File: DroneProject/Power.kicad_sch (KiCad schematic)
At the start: 15 parts, among them SW1 PTS815 SJM 250 SMTR LFS, U31 AP63205WU, U32 TLV75533PDBV

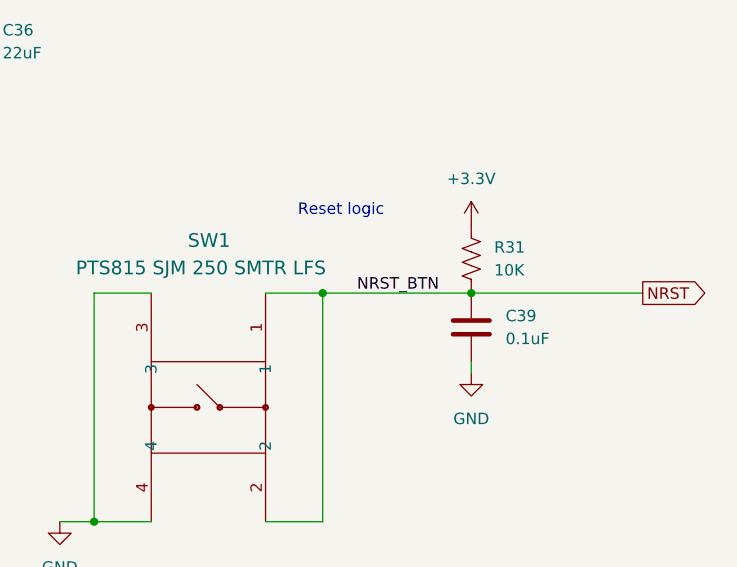
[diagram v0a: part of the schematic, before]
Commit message: Added mounting holes and some more testpoints.  Also started on PCB with dimesions and mounting holes measured and placed
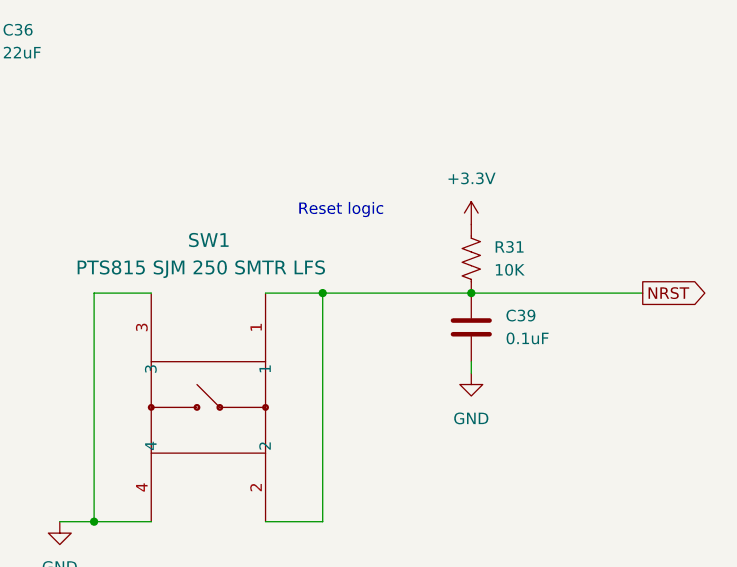
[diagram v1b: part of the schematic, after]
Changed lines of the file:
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@@
-		)
-	)
-	(label "NRST_BTN"
-		(at 212.09 76.2 0)
-		(effects
-			(font
-				(size 1.27 1.27)
-			)
-			(justify left bottom)
 		)
 	)

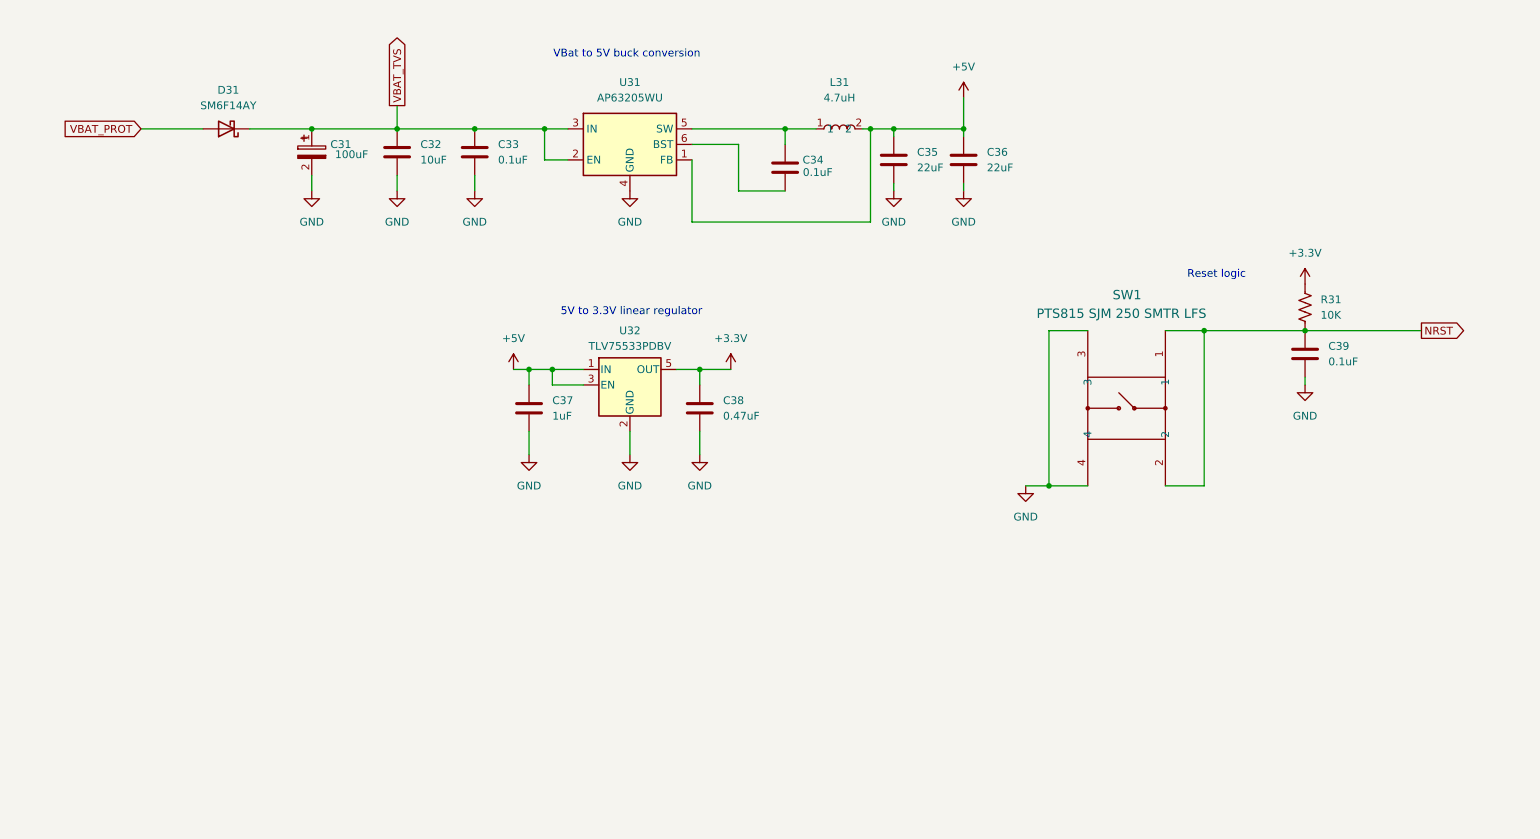
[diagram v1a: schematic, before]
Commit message: Finished initial PCB layout.  However decided to go ahead and add the motor drivers for the first prototype anyways.  Re-did the reverse-polarity detection to use an NMOS instead of a PMOS.  Added sheets for each motor, still need to decide on parts.
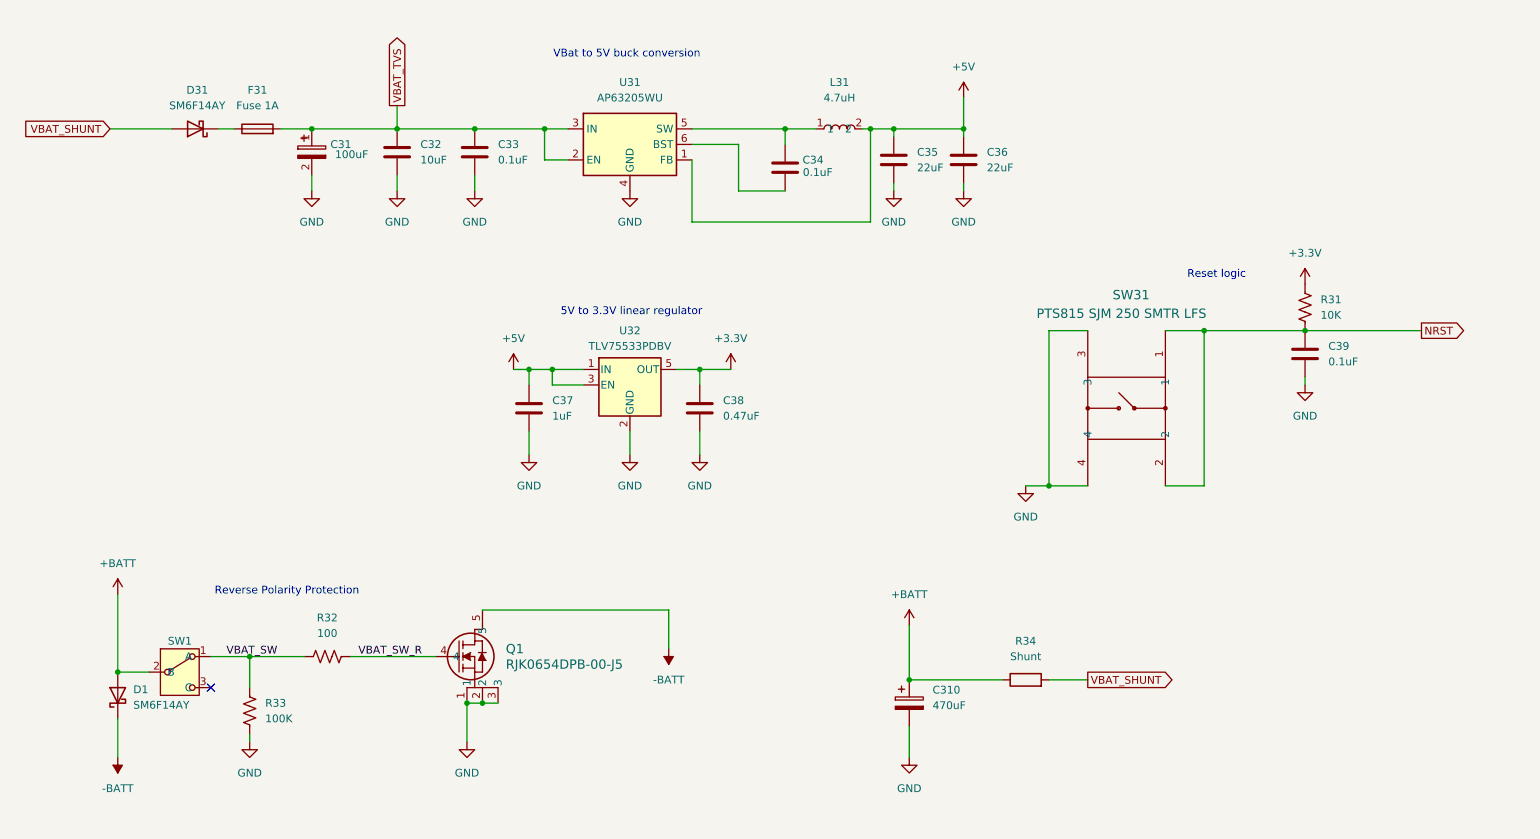
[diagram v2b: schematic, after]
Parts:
- added C310: 470uF, Capacitor_SMD:CP_Elec_10x10.5, symbol Device:C_Polarized
- added D1: SM6F14AY, Diode_SMD:D_SOD-128, symbol Diode:PMEG4050EP
- added F31: Fuse 1A, Fuse:Fuse_1812_4532Metric, symbol Device:Fuse
- added Q1: RJK0654DPB-00-J5, Library:LFPAK_REN, symbol Global:RJK0654DPB-00-J5
- added R32: 100, Resistor_SMD:R_0201_0603Metric, symbol Device:R_US
- added R33: 100K, Resistor_SMD:R_0402_1005Metric, symbol Device:R_US
- added R34: Shunt, Resistor_SMD:R_2010_5025Metric, symbol Device:R
- added SW1: ~, Library:SW_EG1218, symbol Global:EG1903-ND
- renumbered SW1 to SW31
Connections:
- net GND: now also C310.2, Q1.1, Q1.2, Q1.3, R33.2
- net VBAT_TVS: now also F31.2; no longer D31.1 (K)
- net VBAT_PROT renamed VBAT_SHUNT
- net VBAT_SHUNT: now also R34.2
- new net: D31.1 (K), F31.1
- new net +BATT: C310.1, D1.2 (A), R34.1, SW1.2 (B)
- new net -BATT: D1.1 (K), Q1.5
- new net VBAT_SW: R32.1, R33.1, SW1.1 (A)
- new net VBAT_SW_R: Q1.4, R32.2
- no-connect marks 0 -> 1
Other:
- note added: "Reverse Polarity Protection"
- moved on the sheet: D31

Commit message: Re-did layout for new power system
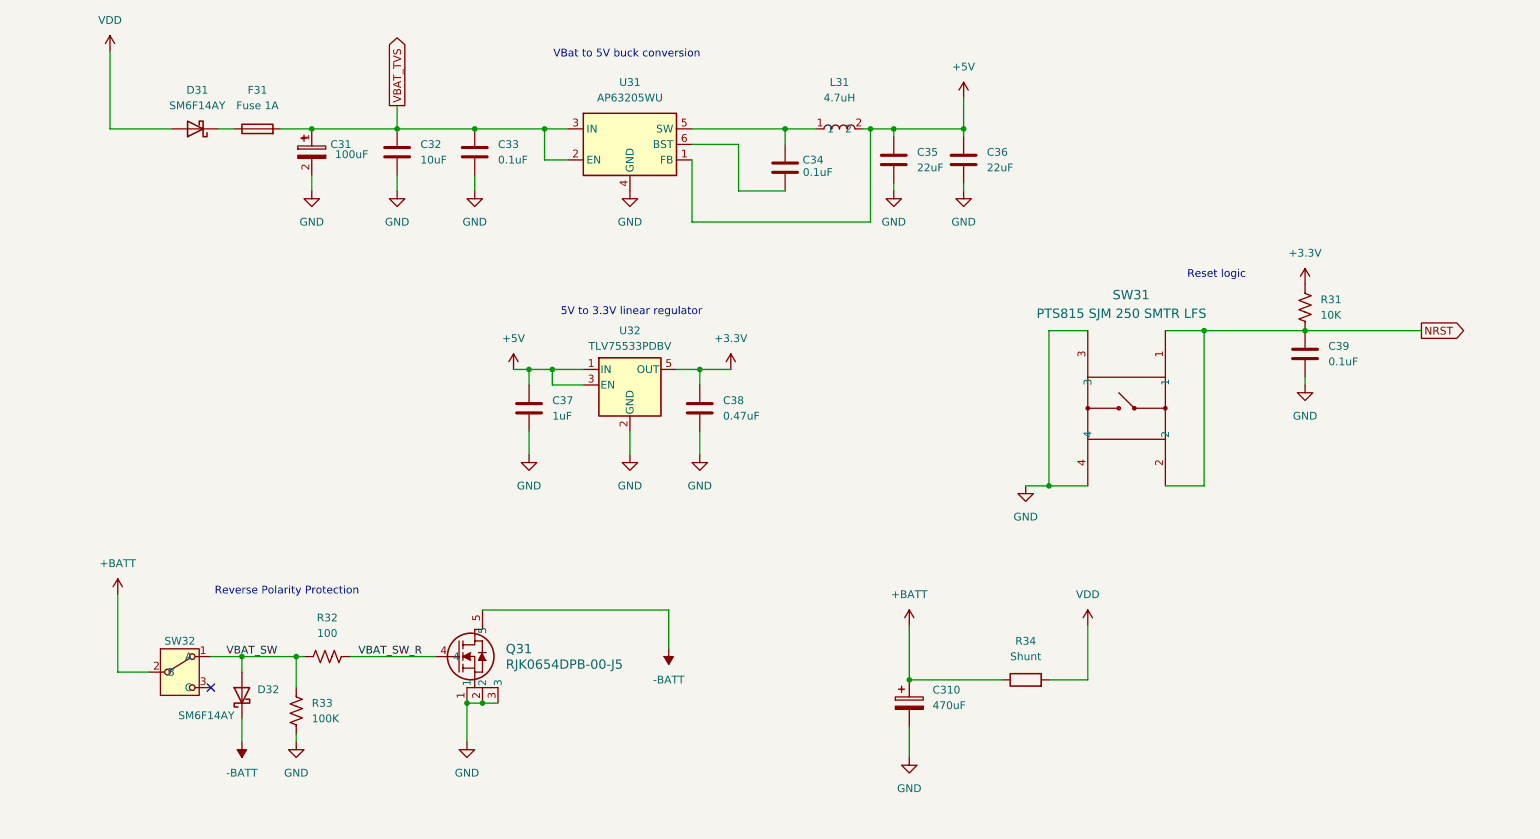
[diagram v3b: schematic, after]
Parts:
- renumbered D1 to D32, Q1 to Q31, SW1 to SW32
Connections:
- net +BATT: no longer D32.2 (A)
- net VBAT_SW: now also D32.2 (A)
- net VBAT_SHUNT renamed VDD
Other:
- moved on the sheet: D32, R33

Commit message: Added a second MCU for motor control.  Removed 5V rail.  Added COM switching for SWD and UART external headers
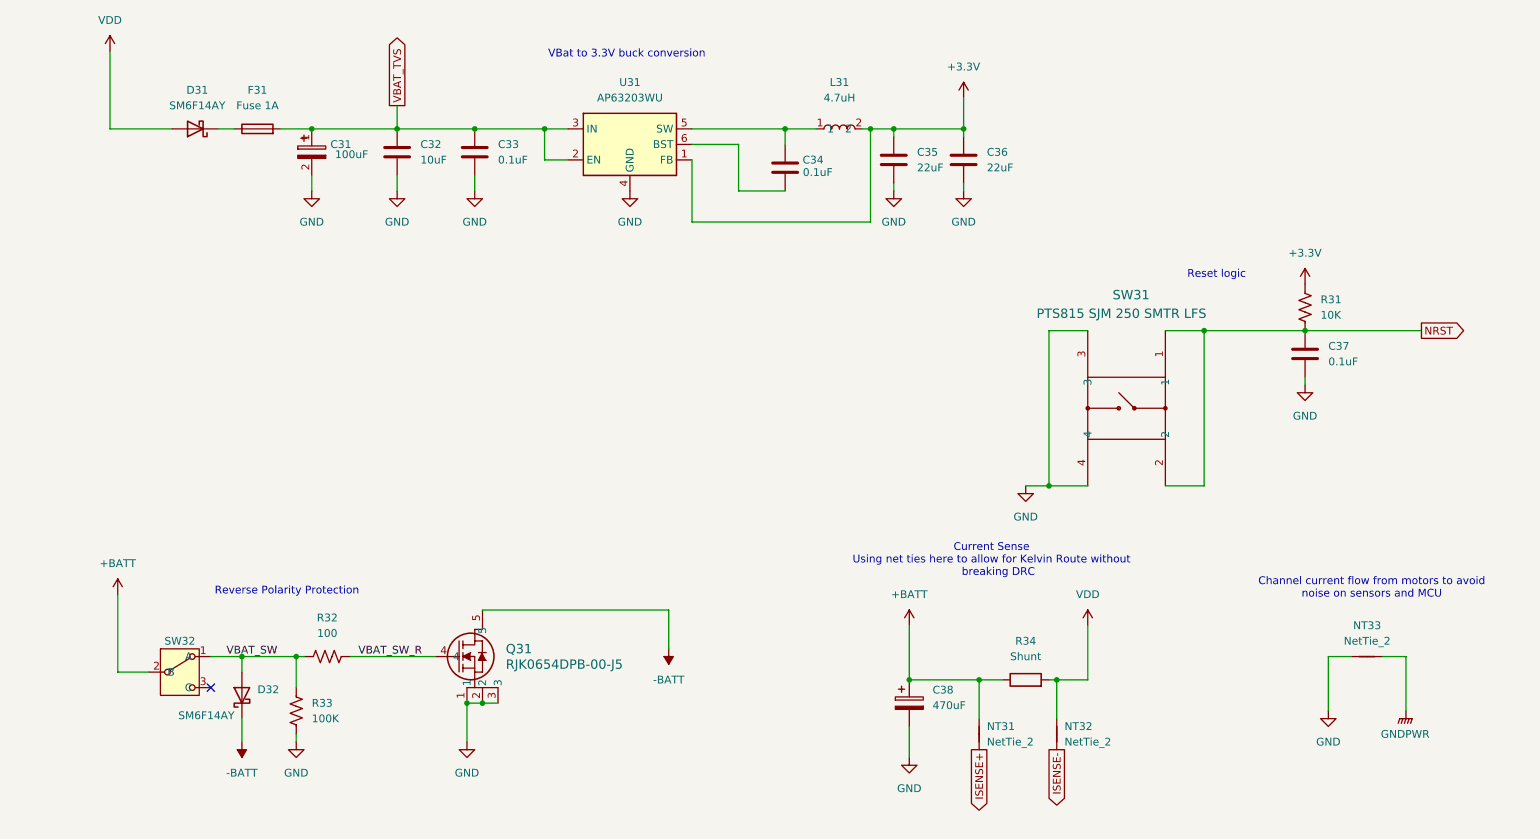
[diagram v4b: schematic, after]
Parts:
- removed C37: 1uF, Capacitor_SMD:C_0402_1005Metric, symbol Device:C
- removed C38: 0.47uF, Capacitor_SMD:C_0402_1005Metric, symbol Device:C
- removed U31: AP63205WU, Package_TO_SOT_SMD:TSOT-23-6, symbol Regulator_Switching:AP63205WU
- removed U32: TLV75533PDBV, Package_TO_SOT_SMD:SOT-23-5, symbol Regulator_Linear:TLV75533PDBV
- added NT31, NT32: NetTie_2, NetTie:NetTie-2_SMD_Pad0.5mm, symbol Device:NetTie_2
- added NT33: NetTie_2, NetTie:NetTie-2_SMD_Pad2.0mm, symbol Device:NetTie_2
- added U31: AP63203WU, Package_TO_SOT_SMD:TSOT-23-6, symbol Regulator_Switching:AP63203WU
- renumbered C39 to C37, C310 to C38
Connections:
- net +5V is gone; now on net +3.3V: C35.1, C36.1, L31.2
- net +3.3V: now also U31.1 (FB)
- net +BATT: now also NT31.2
- net GND: now also NT33.2, U31.4 (GND)
- net VBAT_TVS: now also U31.2 (EN), U31.3 (IN)
- net VDD: now also NT32.2
- net at C34.2, L31.1: now also U31.5 (SW)
- net at C34.1: now also U31.6 (BST)
- new net GNDPWR: NT33.1
- new net ISENSE+: NT31.1
- new net ISENSE-: NT32.1
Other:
- note added: "Channel current flow from motors to avoid noise on sensors and MCU"
- note added: "Current Sense Using net ties here to allow for Kelvin Route without breaking DRC"
- note added: "VBat to 3.3V buck conversion"
- note removed: "5V to 3.3V linear regulator"
- note removed: "VBat to 5V buck conversion"

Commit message: Removed C1 and motor controllers from main platform and moved to own project
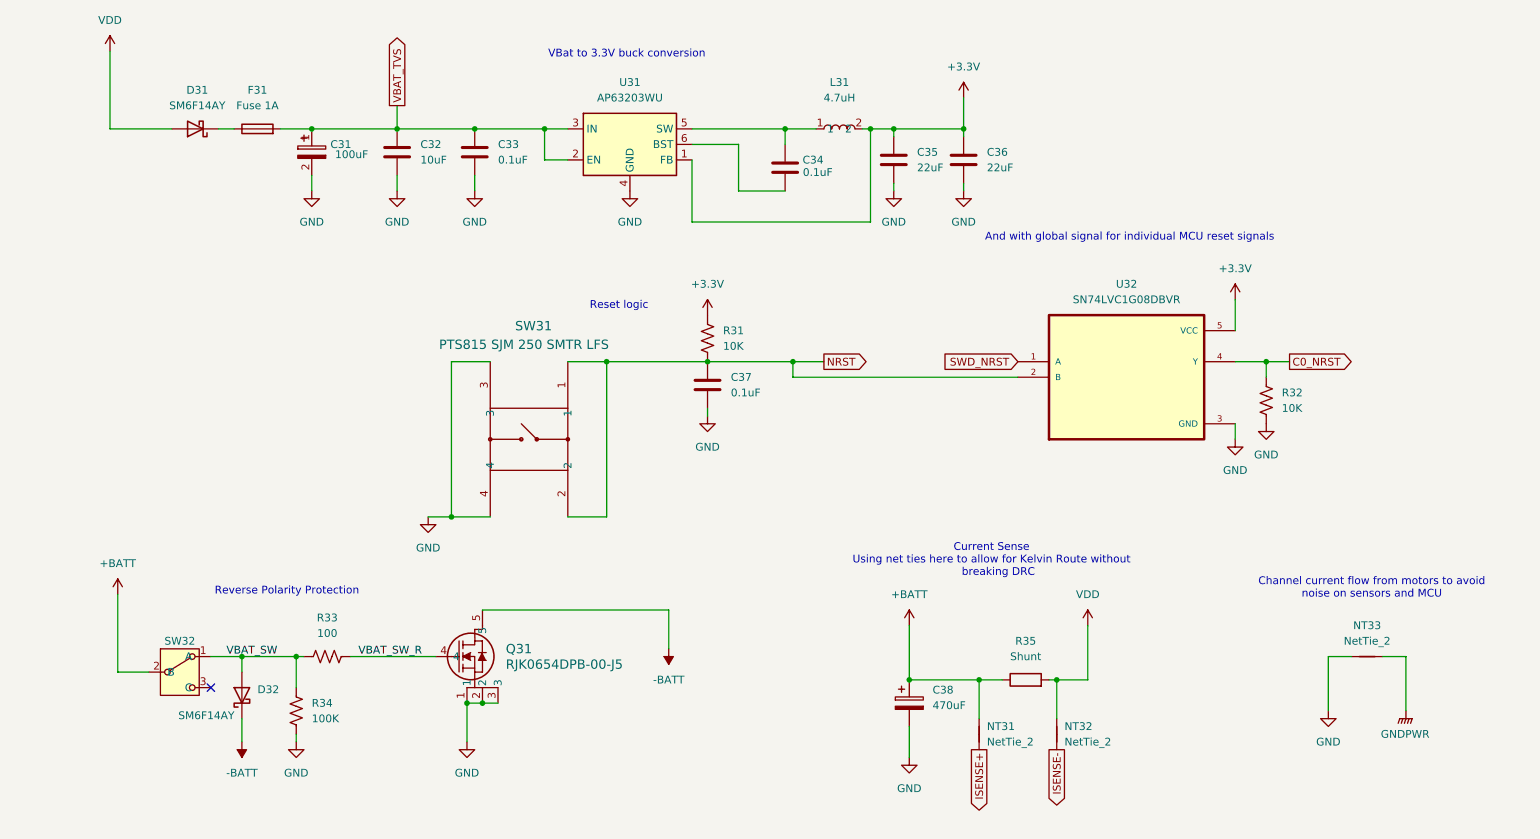
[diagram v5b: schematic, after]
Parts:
- added R32: 10K, Resistor_SMD:R_0402_1005Metric, symbol Device:R_US
- added U32: SN74LVC1G08DBVR, Library:SOT95P280X145-5N, symbol Global:SN74LVC1G08DBVR
- renumbered R32 to R33, R33 to R34, R34 to R35
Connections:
- net +3.3V: now also U32.5 (VCC)
- net GND: now also R32.1, U32.3 (GND)
- net NRST: now also U32.2 (B)
- new net C0_NRST: R32.2, U32.4 (Y)
- new net SWD_NRST: U32.1 (A)
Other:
- note added: "And with global signal for individual MCU reset signals"
- moved on the sheet: C37, R31, SW31

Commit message: Completed schematic for brushless ESC and added needed components to main board.  The plan is to mount the ESCs on the main board using 2.54mm Vert Conn Headers
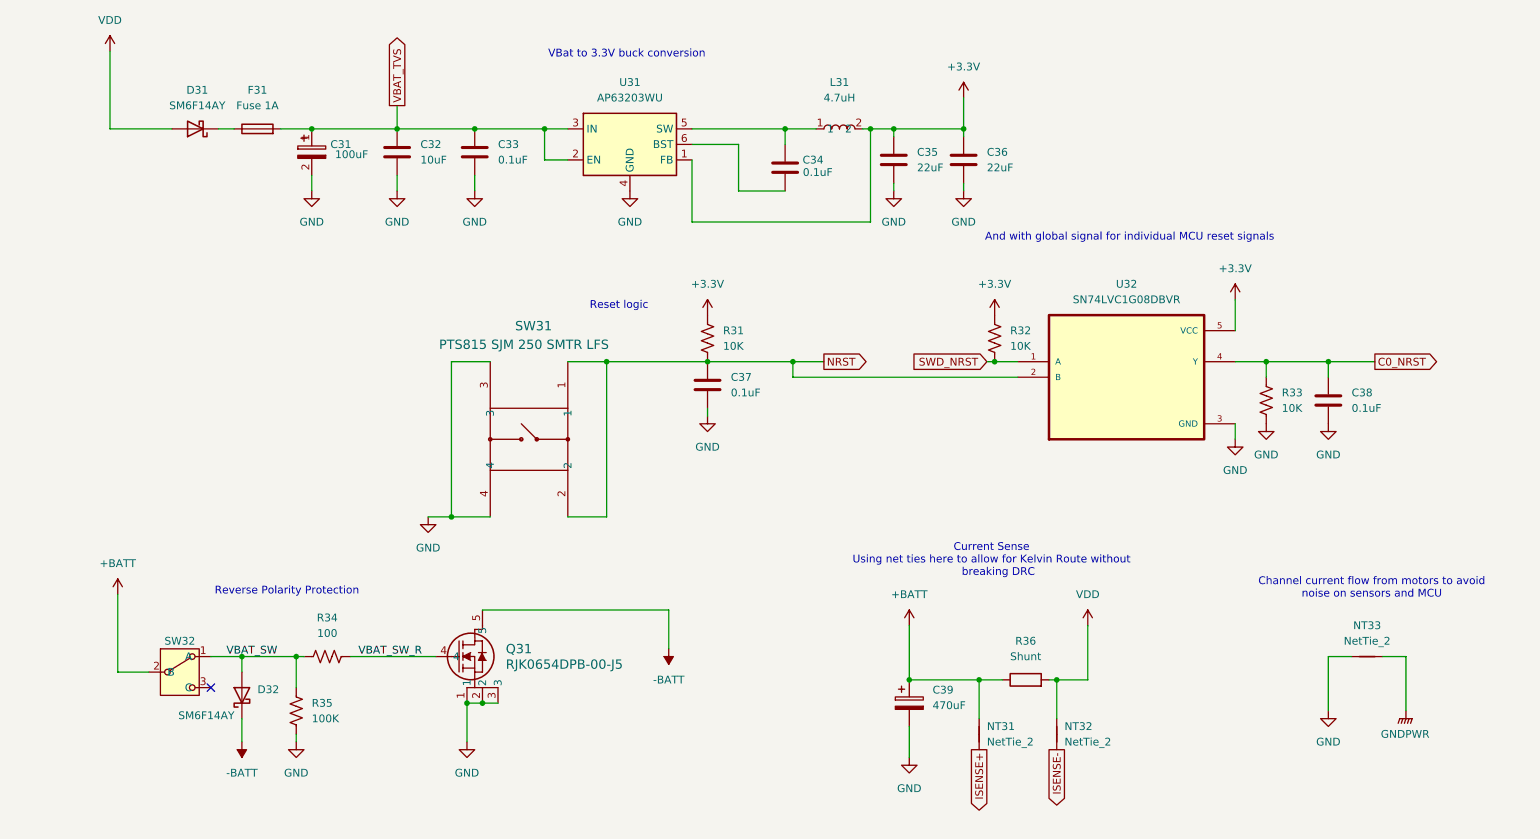
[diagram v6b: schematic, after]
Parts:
- added C38: 0.1uF, Capacitor_SMD:C_0402_1005Metric, symbol Device:C
- added R32: 10K, Resistor_SMD:R_0402_1005Metric, symbol Device:R_US
- renumbered C38 to C39, R32 to R33, R33 to R34, R34 to R35, R35 to R36
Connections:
- net +3.3V: now also R32.2
- net C0_NRST: now also C38.1
- net GND: now also C38.2
- net SWD_NRST: now also R32.1
